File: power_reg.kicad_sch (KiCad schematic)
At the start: 11 parts, among them U2 AZ1117-3.3, U4 AP2112K-1.8

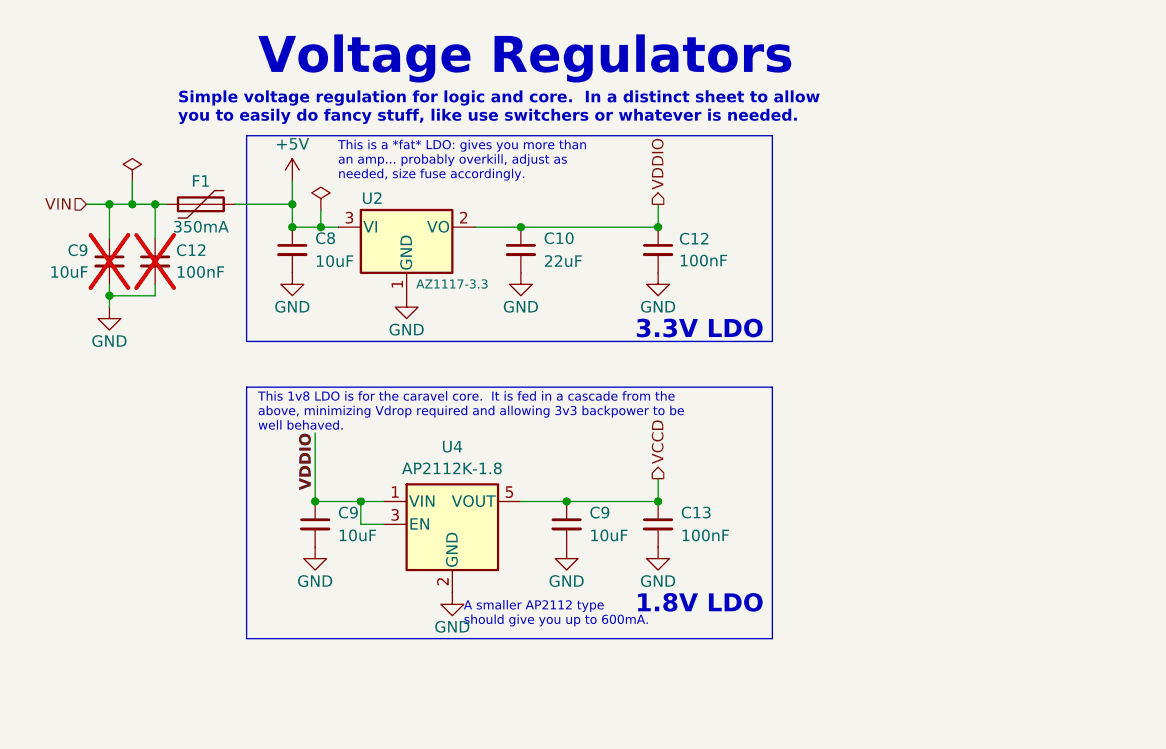
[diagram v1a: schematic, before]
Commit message: Reset rise and slow clock config fixes
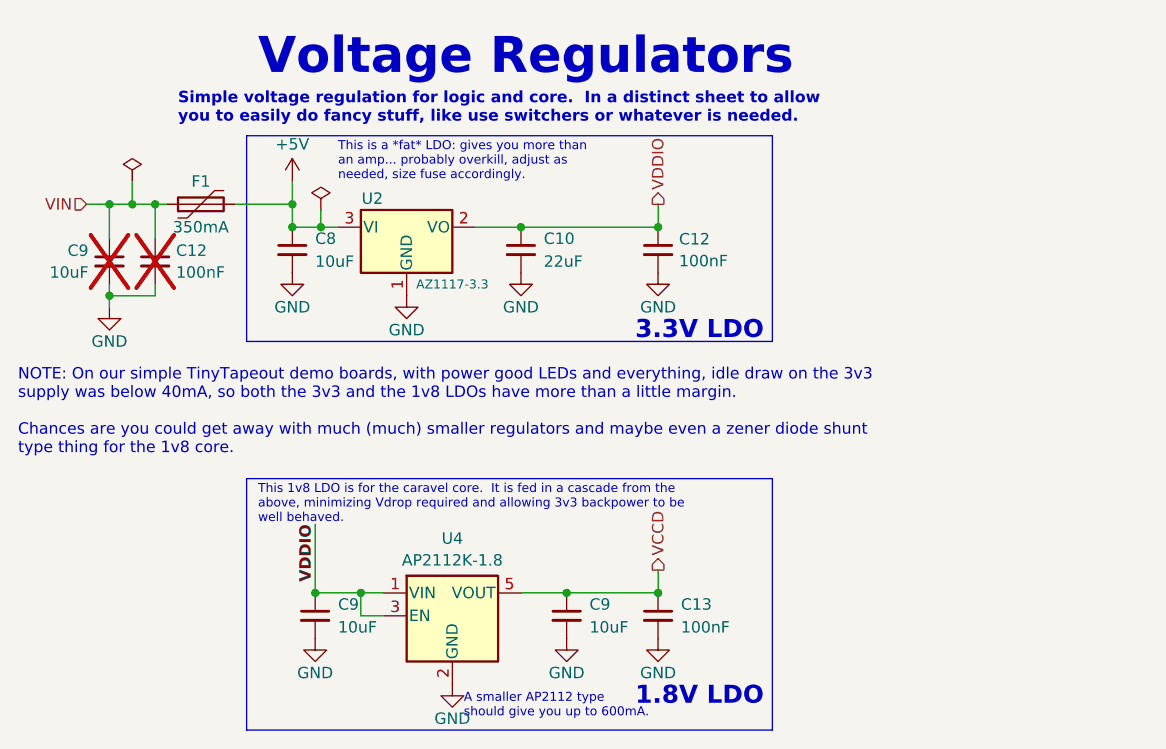
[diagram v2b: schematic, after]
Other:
- note added: "NOTE: On our simple TinyTapeout demo boards, with power good LEDs and everything, idle draw on the 3v3 supply was below 40mA, so both the 3v3 and the 1v8 LDOs have more than a little margin. Chances are you could get away with much (much) smaller regulators and maybe even a zener diode shunt type thing for the 1v8 core."
- moved on the sheet: C13, C9, U4

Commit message: minor cleanups and clarifications
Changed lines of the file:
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@@
   )
   (symbol (lib_id "Device:C_Small") (at 53.34 40.64 0) (unit 1)
-    (in_bom yes) (on_board yes) (dnp no) (fields_autoplaced)
-    (property "Reference" "C8" (at 55.88 39.3762 0)
+    (in_bom yes) (on_board yes) (dnp no)
+    (property "Reference" "C8" (at 48.768 38.862 0)
       (effects (font (size 1.27 1.27)) (justify left))
     )
-    (property "Value" "10uF" (at 55.88 41.9162 0)
+    (property "Value" "10uF" (at 53.594 42.418 0)
       (effects (font (size 1.27 1.27)) (justify left))
     )
@@
   )
   (symbol (lib_id "Device:C_Small") (at 55.88 81.28 0) (unit 1)
-    (in_bom yes) (on_board yes) (dnp no) (fields_autoplaced)
-    (property "Reference" "C9" (at 58.42 80.0162 0)
+    (in_bom yes) (on_board yes) (dnp no)
+    (property "Reference" "C9" (at 51.308 79.502 0)
       (effects (font (size 1.27 1.27)) (justify left))
     )
-    (property "Value" "10uF" (at 58.42 82.5562 0)
+    (property "Value" "10uF" (at 56.134 83.058 0)
       (effects (font (size 1.27 1.27)) (justify left))
     )
